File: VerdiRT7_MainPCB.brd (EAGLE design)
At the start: 146 x 66 mm, 183 parts, among them J1 RECEPT_SMD_5-2, J2 RECEPT_SMD_5-2, J4 MOLEX_105027, J5 BM06B-SRSS-TB, J8 BM02B-SRSS-TB, J9 BM02B-ZESS-TBT, Q1 AON7934, Q14 AON7934, Q15 AON7934, Q2 AON7934, Q3 AON7934, Q4 AON7934, Q7 SI7615ADN, SW1 AYZ0102AGRLC, SW3 SKRH, SW4 TACT_SWITCHO, U10 RT9625A, U13 MCP1416, U14 MCP1416, U15 MCP1416, U16 MCP6001, U17 MCP6001, U18 RT9625A, U2 MPU-6500, U3 7408_3, U4 RT9625A, U5 MCP6001, U6 MCP1416, U7 7408_3, U8 7408_3, U9 MCP6001, X1 NX3225

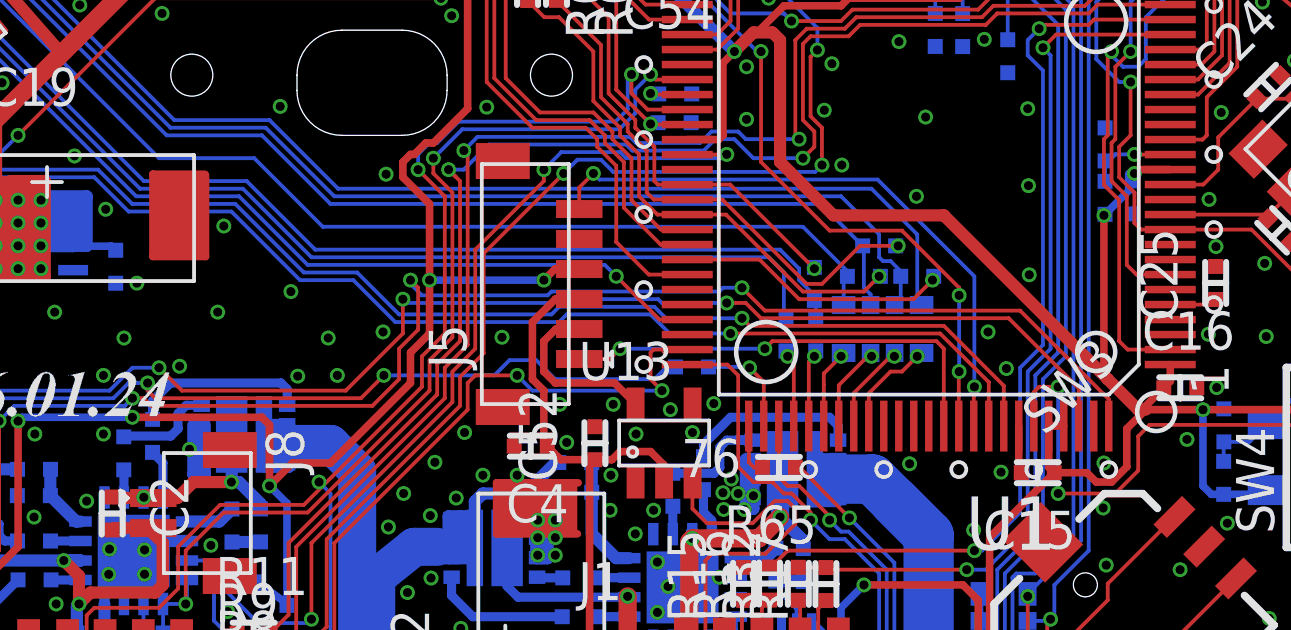
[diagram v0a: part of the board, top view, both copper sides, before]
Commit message: updated: AD0 モジュール使用によるピンアサイン変更          P05, P07 を使用しない
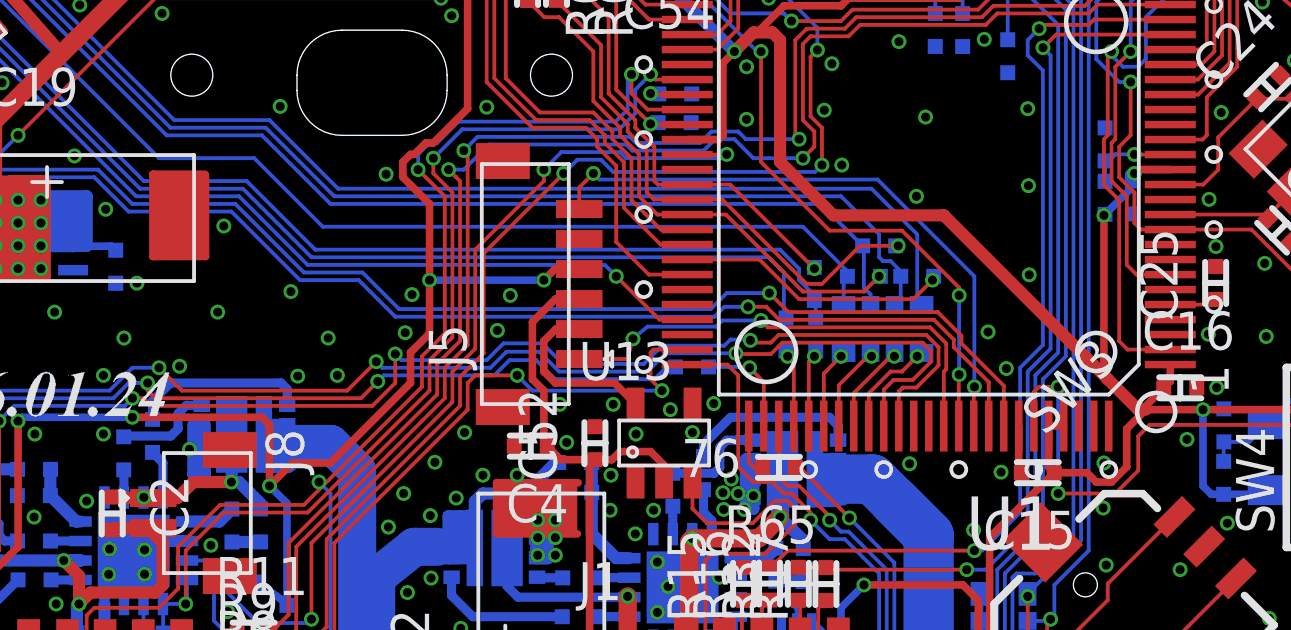
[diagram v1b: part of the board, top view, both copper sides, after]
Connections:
- net MOTOR1: now also U1.86; no longer U1.100
- net MOTOR2: now also U1.85; no longer U1.98
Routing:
- net MOTOR1: track 55.3 -> 49.2 mm
- net MOTOR2: track 54.7 -> 50.3 mm
- net AD_ASEN1: track 15.1 -> 16.1 mm
- net GND: vias 334 -> 336

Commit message: updated: schematic にコメント挿入
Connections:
- net N$86 renamed PWM_MOT1_MPU
- net N$87 renamed PWM_MOT2_MPU
- net N$88 renamed PWM_MOT3_MPU
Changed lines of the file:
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@@
 <wire x1="73.7554" y1="34.4486" x2="73.7554" y2="33.7084" width="0.127" layer="16"/>
 </signal>
-<signal name="N$86">
+<signal name="PWM_MOT1_MPU">
 <contactref element="U1" pad="77"/>
 <contactref element="R62" pad="P$2"/>
@@
 <via x="85.598" y="15.24" extent="1-16" drill="0.3" shape="octagon"/>
 </signal>
-<signal name="N$87">
+<signal name="PWM_MOT2_MPU">
 <contactref element="U1" pad="76"/>
 <contactref element="R65" pad="P$2"/>
@@
 <wire x1="85.5708" y1="12.0922" x2="85.5708" y2="13.2961" width="0.127" layer="1"/>
 </signal>
-<signal name="N$88">
+<signal name="PWM_MOT3_MPU">
 <contactref element="R66" pad="P$2"/>
 <contactref element="U1" pad="46"/>

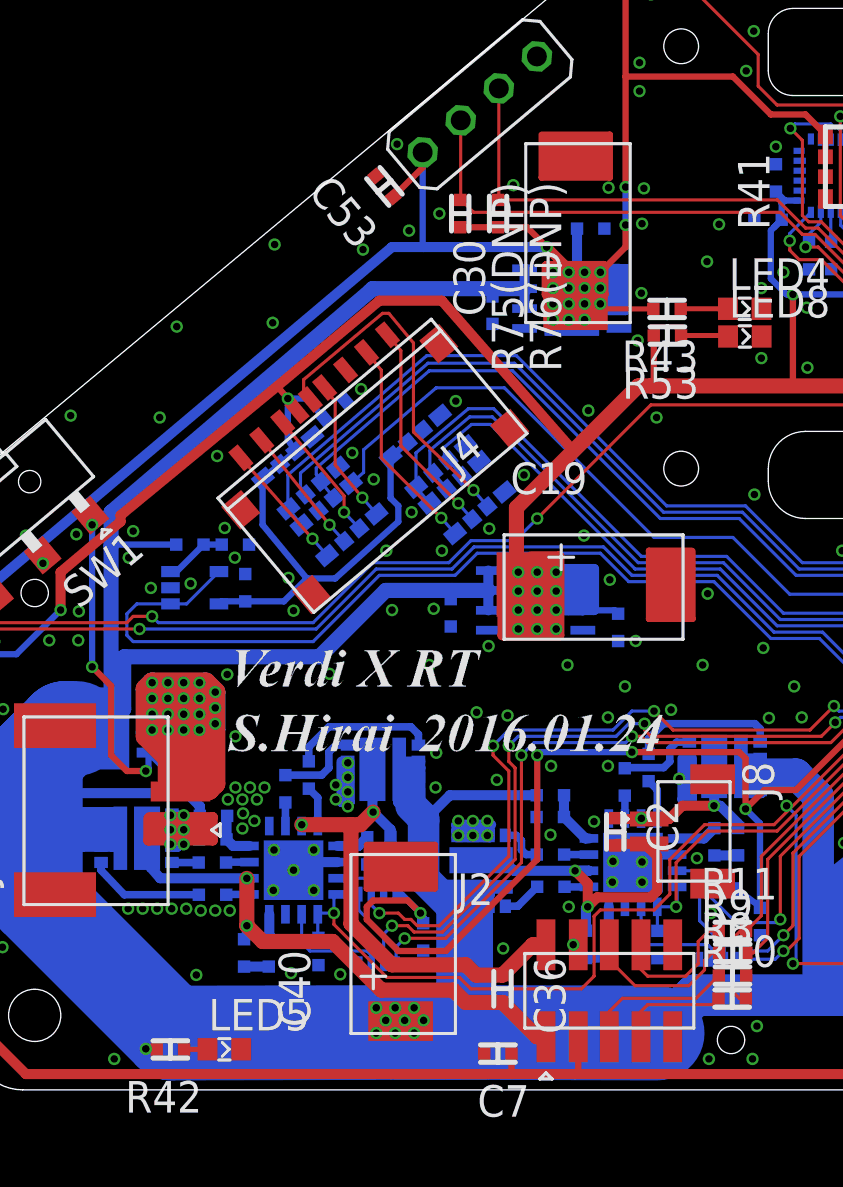
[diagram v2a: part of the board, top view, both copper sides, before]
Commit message: updated: Bluetooth モジュールの電源を+5V -> +3.3V に変更
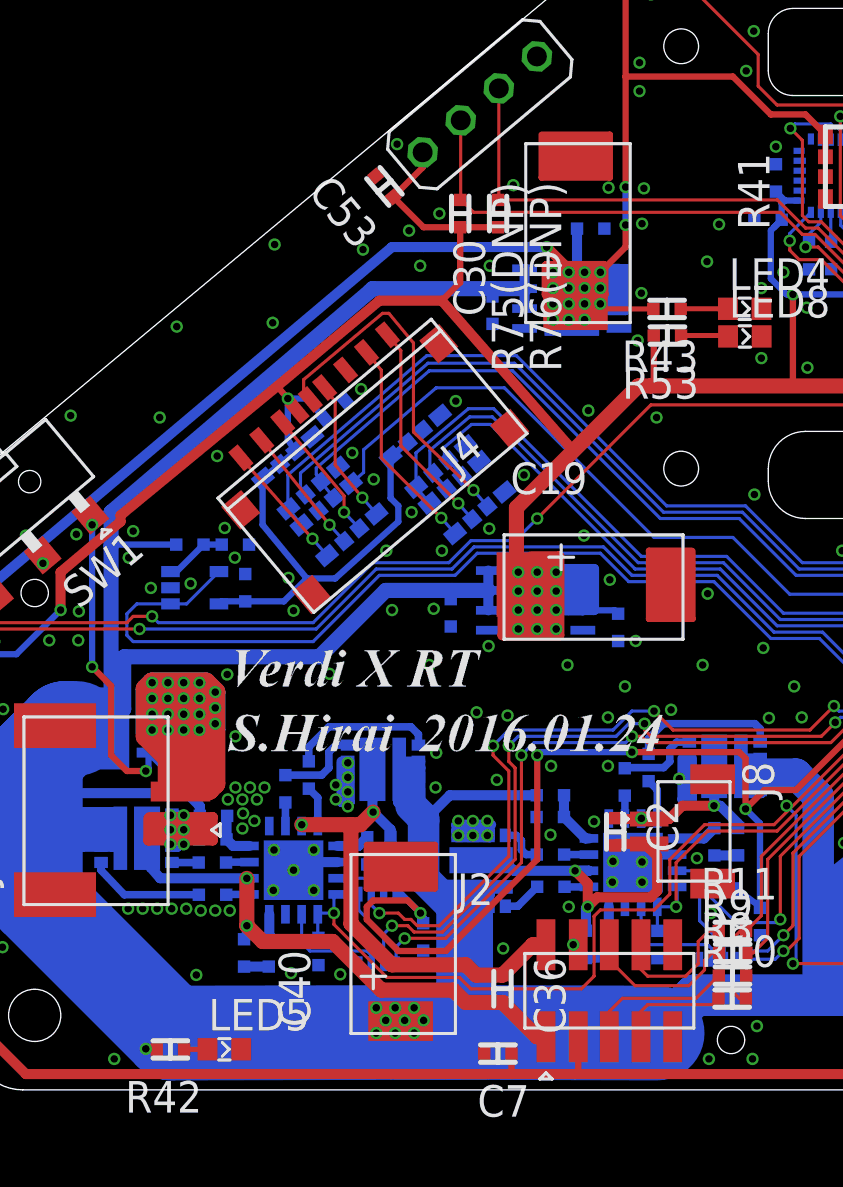
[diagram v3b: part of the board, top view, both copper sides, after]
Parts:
- R10, R15, R32, R8: value 0 -> 0 (DNP)
- R21, R22: value 20k -> 20k (DNP)
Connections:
- net +3V3: now also C53.P$1, CH1.1, R75(DNP).P$2, R76(DNP).P$2
- net +5V: no longer C53.P$1, CH1.1, R75(DNP).P$2, R76(DNP).P$2
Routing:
- net +3V3: track 443.4 -> 454.4 mm
- net +5V: track 255.6 -> 253.8 mm
- net GND: track 75.7 -> 75.8 mm, vias 336 -> 338
- added copper zone on layer 1, net +8V
- added copper zone on layer 1, net VCC

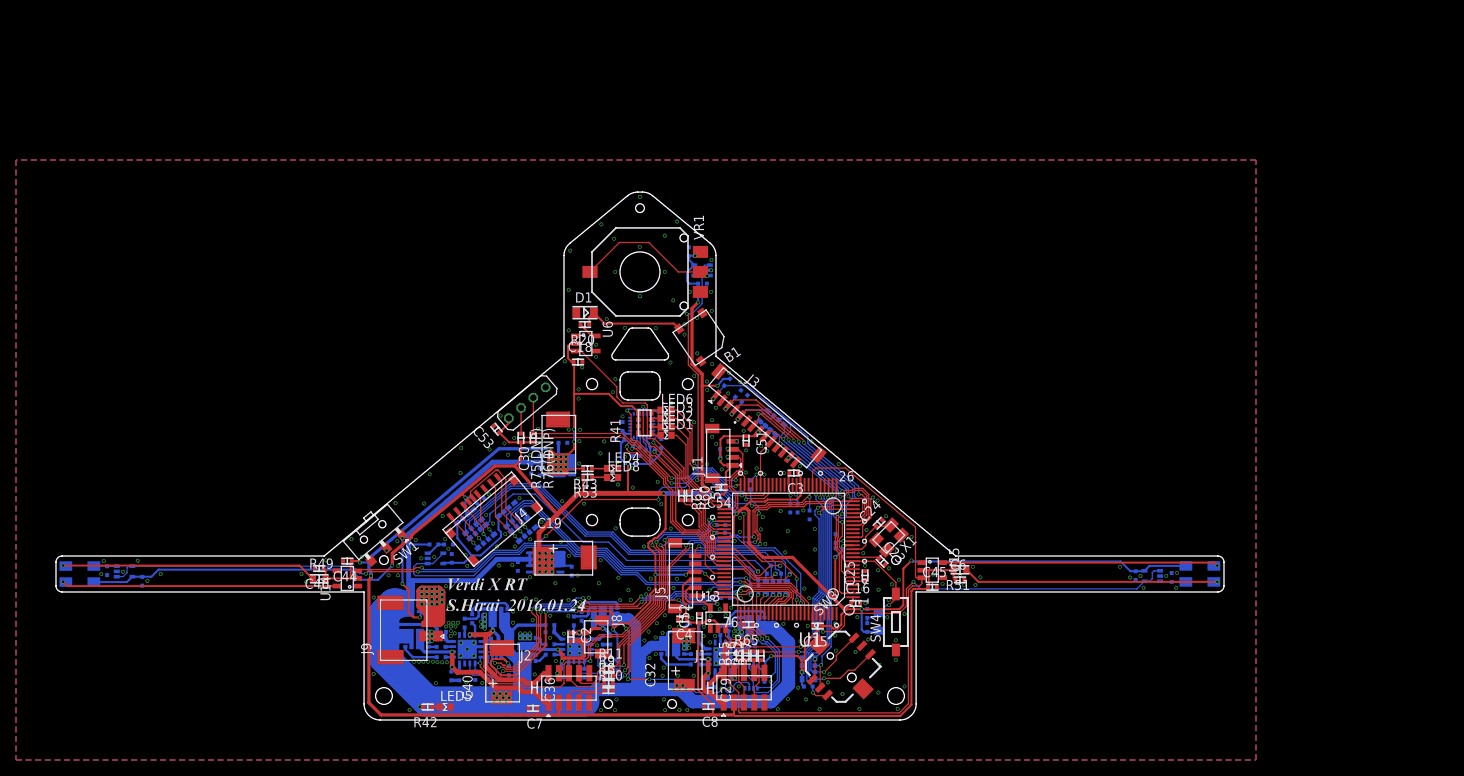
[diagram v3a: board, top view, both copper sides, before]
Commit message: updated: コネクタ変更，ディスコンFET 交換
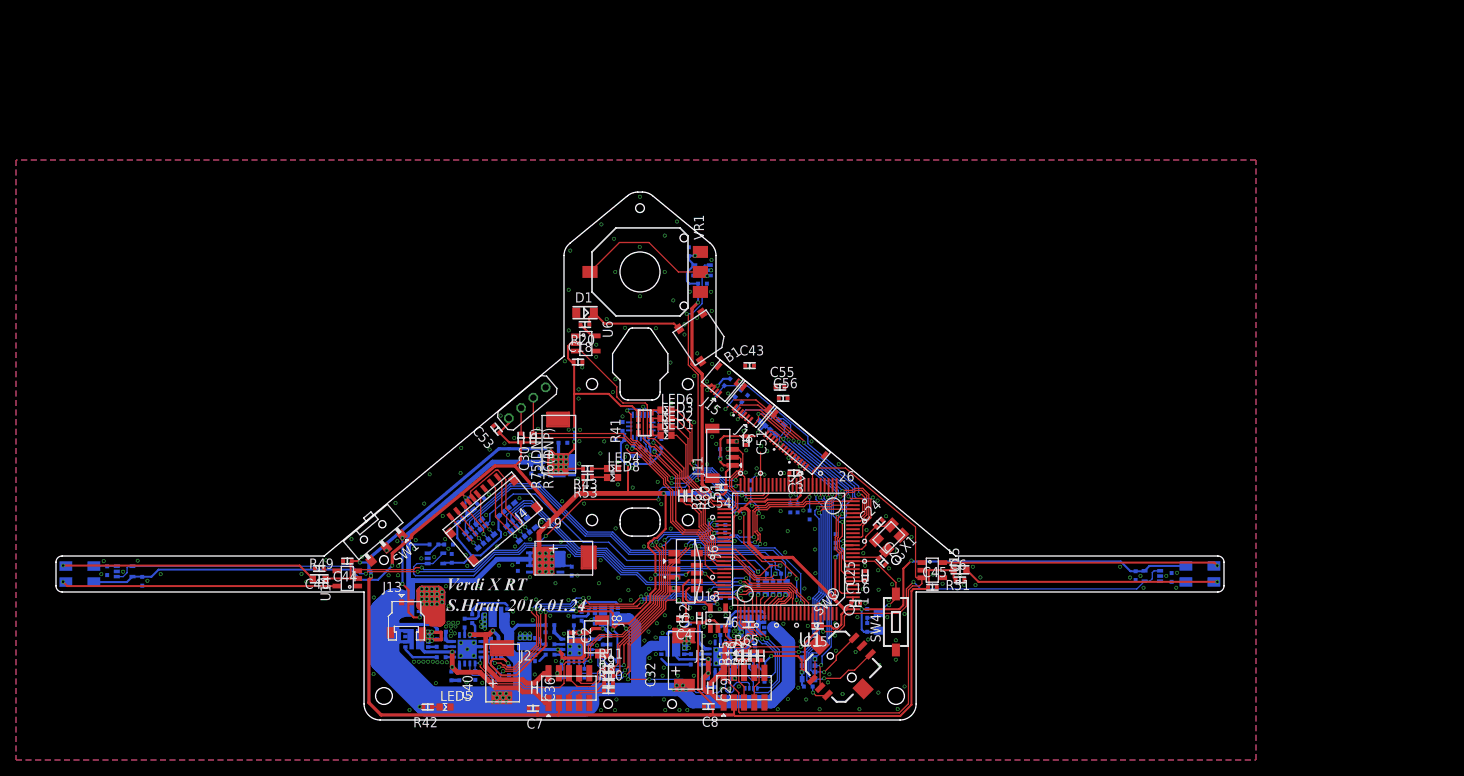
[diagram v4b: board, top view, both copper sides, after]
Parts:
- removed J3: (no value), jst_sh:BM14B-SRSS-TB
- removed J5: BM06B-SRSS-TB, jst_sh:BM06B-SRSS-TB
- removed J9: BM02B-ZESS-TBT, jst_ze:BM02B-ZESS-TBT
- removed Q14, Q15, Q4: AON7934, MOSFET:DFN3X3A
- removed U2: MPU-6500, gyro:QFN24_0.4MM
- added C43: 16V 1u, capacitor:1005
- added C55, C56: 10V 1u, capacitor:1005
- added J13: DF58_2P, Hirose_DF:DF58_2P
- added J15: 503480_0400, molex_503480:0400
- added J16: 503480_0600, molex_503480:0600
- added J6: 52559-0652, molex_52559:0652
- added J7: 503480_1400, molex_503480:1400
- added Q5, Q6, Q8: SIZ322DT, MOSFET:DFN3X3A
- added U19: ICM-20602, ICM-2060x:LGA16_3X3MM
- C19, C30: value 16V68u -> 16V33u
- C32, C40: value 16V 68u -> 16V 33u
- Q1, Q2, Q3: value AON7934 -> SIZ322DT
- moved Q1 18.4 mm to (68.8, 13.0)
- moved Q2 18.2 mm to (58.9, 8.80), turned to 0 degrees
- moved Q3 10.3 mm to (45.1, 10.1), turned to 90 degrees
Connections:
- removed net N$21: J5.2, U13.5
- new net 7_RESV: U19.7
- new net IO_SPARE0: J16.3, U1.39
- new net IO_SPARE1: J16.4, U1.40
- new net IO_SPARE2: J16.5, U1.41
- new net IO_SPARE3: J15.2, U1.47
- new net IO_SPARE4: J15.3, U1.48
- new net N$5: R49.P$2, U14.5
- net +3V3: now also C4.P$1, C55.P$1, J16.2, J6.4, J7.8, U19.1, U19.16; no longer J3.8, J5.4, U2.13, U2.8
- net +5V: now also C56.P$1, J16.1; no longer C4.P$1, J5.3, R49.P$2, R51.P$2
- net +8V: now also C43.P$1, J15.1, Q5.2, Q5.3, Q5.4, Q5.PAD_S, Q6.2, Q6.3, Q6.4, Q6.PAD_S, Q8.2, Q8.3, Q8.4, Q8.PAD_S; no longer Q14.2, Q14.3, Q14.4, Q14.PAD_S, Q15.2, Q15.3, Q15.4, Q15.PAD_S, Q4.2, Q4.3, Q4.4, Q4.PAD_S
- net AD_ASEN1: now also J6.1; no longer J5.1
- net AD_ASEN2: now also J6.6; no longer J5.6
- net EMLE: now also J7.4; no longer J3.4
- net GND: now also C43.P$2, C55.P$2, C56.P$2, J13.2, J13.CASE_1, J13.CASE_2, J15.4, J15.CASE1, J15.CASE2, J16.6, J16.CASE1, J16.CASE2, J6.2, J6.5, J6.CASE1, J6.CASE2, J6.CASE3, J6.CASE4, J7.12, J7.14, J7.2, J7.CASE1, J7.CASE2, PI1.CATHODE, PI2.CATHODE, Q8.5, Q8.6, Q8.7, U19.10, U19.11, U19.12, U19.13, U19.15, U19.9; no longer J3.12, J3.14, J3.2, J3.PAD1, J3.PAD2, J5.5, J5.PAD1, J5.PAD2, J9.1, J9.PAD1, J9.PAD2, Q1.5, Q1.6, Q1.7, Q14.5, Q14.6, Q14.7, Q15.5, Q15.6, Q15.7, Q4.5, Q4.6, Q4.7, U2.18
- net G_FSYNC: now also U19.8; no longer U2.11
- net G_INT: now also U19.6; no longer U2.12
- net MD/FINE: now also J7.7; no longer J3.7
- net MOT1_OUTA: now also Q5.PAD_L; no longer Q3.PAD_L
- net MOT1_OUTB: now also Q3.PAD_L; no longer Q4.PAD_L
- net MOT2_OUTA: now also Q6.PAD_L; no longer Q1.PAD_L
- net MOT2_OUTB: now also Q8.PAD_L; no longer Q2.PAD_L
- net N$10: now also Q2.8; no longer Q15.8
- net N$2: now also J6.3, U13.5; no longer PI1.CATHODE, U14.5
- net N$37: now also Q6.8; no longer Q1.8
- net N$39: now also Q6.1; no longer Q1.1
- net N$4: now also U19.14; no longer U2.10
- net N$41: now also Q8.1; no longer Q2.1
- net N$42: now also Q8.8; no longer Q2.8
- net N$54: now also R51.P$2; no longer PI2.CATHODE
- net N$61: now also Q5.8; no longer Q3.8
- net N$65: now also Q1.PAD_L; no longer Q14.PAD_L
- net N$73: now also Q5.1; no longer Q3.1
- net N$77: now also Q1.8; no longer Q14.8
- net N$8: now also Q2.PAD_L; no longer Q15.PAD_L
- net N$80: now also Q1.1; no longer Q14.1
- net N$81: now also Q3.1; no longer Q4.1
- net N$82: now also Q3.8; no longer Q4.8
- net N$85: now also U19.4; no longer U2.9
- net N$9: now also Q2.1; no longer Q15.1
- net RESET: now also J7.13; no longer J3.13
- net SPI_CS0: now also U19.5; no longer U2.22
- net SPI_MOSI: now also U19.3; no longer U2.24
- net SPI_SCK: now also U19.2; no longer U2.23
- net TCK: now also J7.1; no longer J3.1
- net TDI: now also J7.11; no longer J3.11
- net TDO: now also J7.5; no longer J3.5
- net TMS: now also J7.9; no longer J3.9
- net TRST#: now also J7.3; no longer J3.3
- net UB: now also J7.10; no longer J3.10
- net VCC: now also J13.1; no longer J9.2
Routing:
- net N$5: track 0.00 -> 34.5 mm, vias 0 -> 1
- net N$2: track 34.8 -> 5.09 mm, vias 1 -> 0
- net +8V: track 243.2 -> 224.8 mm
- net +5V: track 253.8 -> 244.2 mm
- net N$21: track 5.87 -> 0.00 mm
- net GND: track 75.8 -> 71.7 mm
- net +3V3: track 454.4 -> 457.0 mm
- net UB: track 5.94 -> 4.07 mm
- net MOT1_OUTA: track 19.3 -> 17.7 mm
- net AD_ASEN1: track 16.1 -> 14.5 mm
- net N$65: track 7.86 -> 6.27 mm
- net MOT2_OUTB: track 13.5 -> 12.2 mm
- net G_INT: track 24.7 -> 23.5 mm
- net N$4: track 1.21 -> 0.02 mm
- net MOT1_OUTB: track 22.1 -> 20.9 mm
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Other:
- outline, holes or cut-outs redrawn

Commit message: updated: DRC 終了
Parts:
- removed CH1: 1X4P, pin_header_2mm:1X4P
- added C57: 10V 0.1u, capacitor:1005
- added J3: DF13-4P-1.25DSA, Hirose_DF:DF13_4P_TH
- added R64, R74: 100k, resistor:1005
- added R75: 22, resistor:1005
- added U2: MR20H40, Memory:8DFN
- moved R54 13.7 mm to (95.0, 34.2), turned to 40 degrees
- moved C10 10.3 mm to (80.8, 35.0), turned to 90 degrees
- moved C51 10.2 mm to (84.7, 24.9), flipped to the bottom, turned to 225 degrees
- moved R55 10.2 mm to (90.2, 31.9), flipped to the top, turned to 320 degrees
- moved C42 9.95 mm to (80.1, 33.1), turned to 180 degrees
- moved R56 8.92 mm to (90.8, 32.6), flipped to the top, turned to 320 degrees
- moved C55 7.73 mm to (83.2, 39.1), turned to 140 degrees
- moved C26 7.70 mm to (80.2, 36.4), turned to 180 degrees
- moved C4 6.42 mm to (80.9, 18.5), turned to 90 degrees
- moved U19 4.48 mm to (77.2, 34.9), turned to 90 degrees
- moved C21 4.16 mm to (79.8, 35.0)
- moved R57 3.37 mm to (92.4, 35.4), turned to 40 degrees
- moved C43 3.20 mm to (84.2, 42.3), flipped to the bottom, turned to 130 degrees
- moved R3 3.17 mm to (74.2, 35.9), turned to 270 degrees
- moved R63 3.11 mm to (76.5, 31.4), turned to 270 degrees
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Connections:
- new net N$16: R64.P$1, U2.7
- new net N$21: R74.P$1, U2.3
- new net N$45: R75.P$2, U2.2
- net +3V3: now also C57.P$1, J3.1, R64.P$2, R74.P$2, U2.8; no longer CH1.1
- net GND: now also C57.P$2, J13.1, J3.4, Q1.5, Q1.6, Q1.7, Q5.5, Q5.6, Q5.7, Q6.5, Q6.6, Q6.7, U2.4, U2.PAD; no longer CH1.4, J13.2
- net RXD2_BTM: now also J3.3; no longer CH1.3
- net SPI_CS1: now also U2.1
- net SPI_MISO: now also R75.P$1
- net SPI_MOSI: now also U2.5
- net SPI_SCK: now also U2.6
- net TXD2_BTM: now also J3.2; no longer CH1.2
- net VCC: now also J13.2; no longer J13.1
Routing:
- net +8V: track 224.8 -> 268.8 mm, vias 15 -> 20
- net N$54: track 35.6 -> 2.85 mm, vias 1 -> 0
- net N$5: track 34.5 -> 2.80 mm, vias 1 -> 0
- net SPI_CS1: track 0.00 -> 26.1 mm, vias 0 -> 1
- net +5V: track 244.2 -> 267.0 mm, vias 20 -> 22
- net +3V3: track 457.0 -> 476.4 mm, vias 35 -> 36
- net TCK: track 29.8 -> 15.4 mm
- net IO_SPARE4: track 0.00 -> 14.3 mm
- net VCC: track 43.5 -> 29.4 mm
- net IO_SPARE3: track 0.00 -> 14.1 mm
- net TDO: track 27.4 -> 15.2 mm, vias 3 -> 2
- net IO_SPARE2: track 0.00 -> 11.8 mm
- net IO_SPARE1: track 0.00 -> 11.6 mm
- net IO_SPARE0: track 0.00 -> 11.4 mm
- net SPI_MISO: track 23.3 -> 33.4 mm, vias 2 -> 4
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- removed copper zone on layer 1, net VCC
